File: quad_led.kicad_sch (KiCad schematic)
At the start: 8 parts

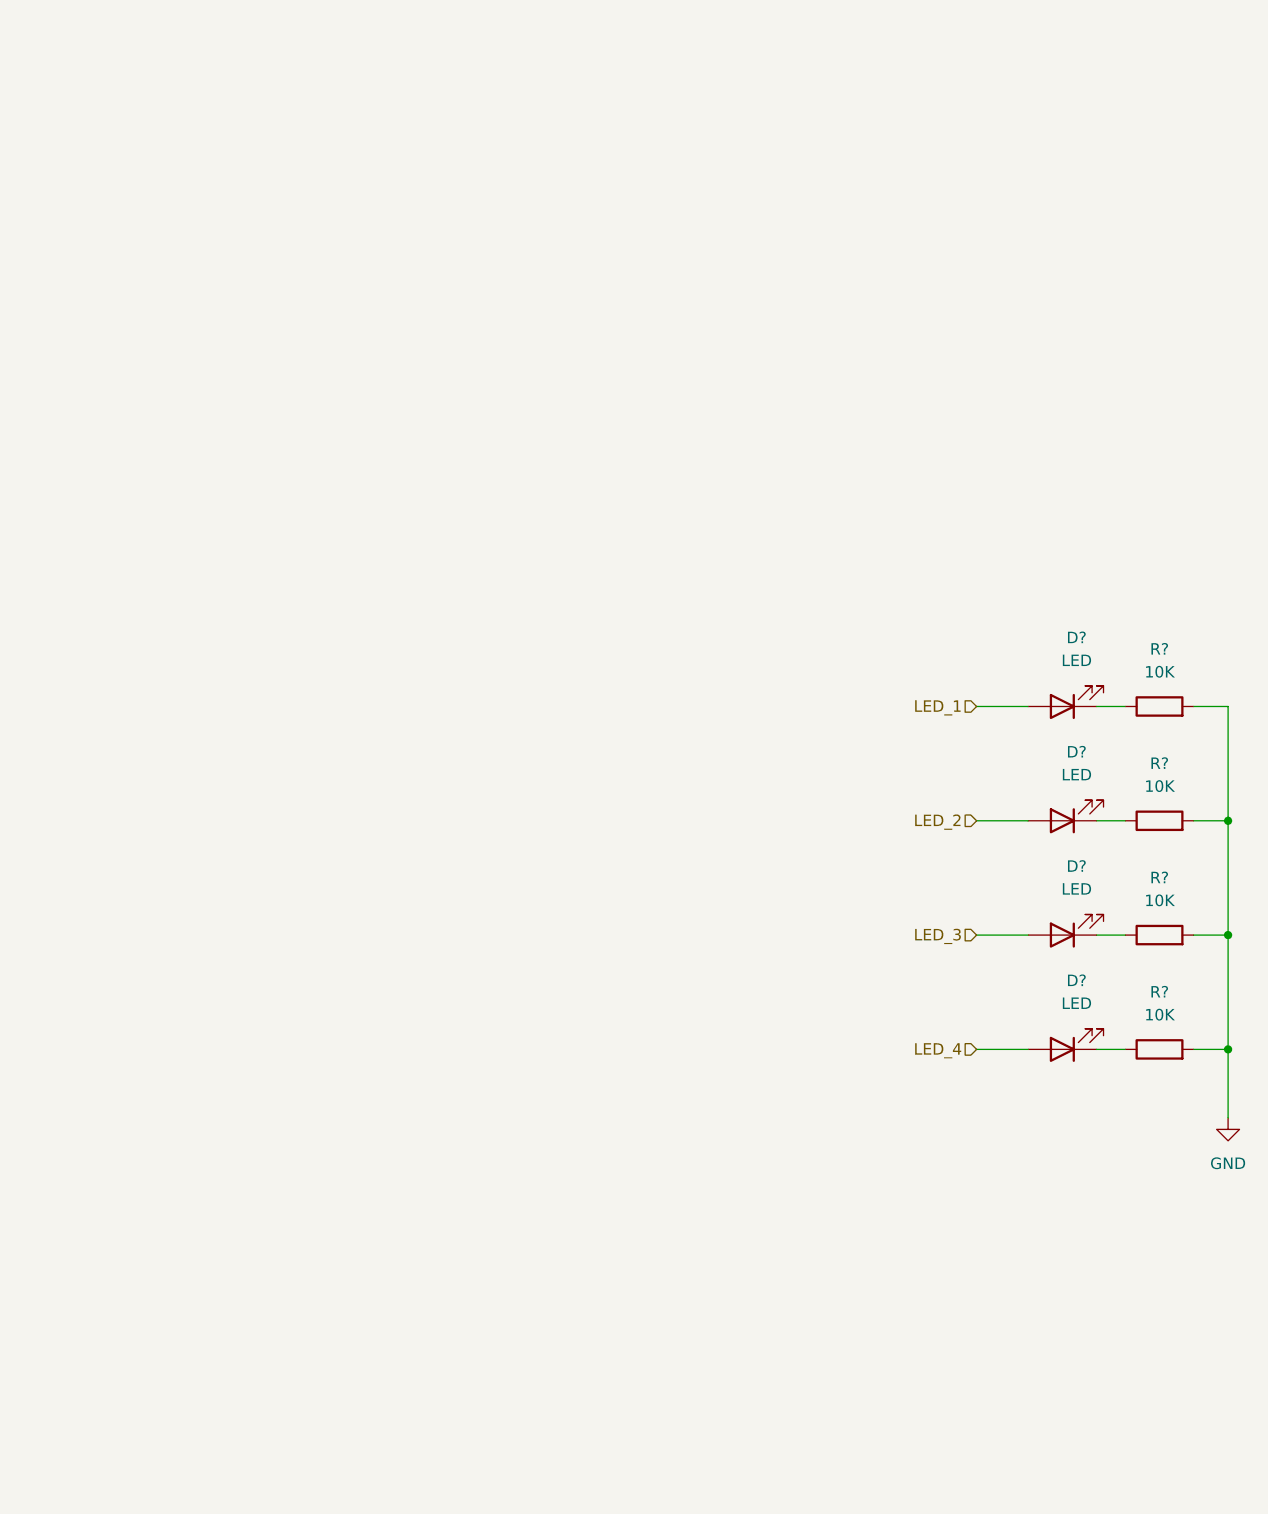
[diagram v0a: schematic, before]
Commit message: Review fixes
- swapped to HC components
- removed ctn_enable
- all 12 LEDs merged into 1 sheet
- No more error with the electrical checker
- various style improvements
- Introduce sleep deprivation errors like calling tranceivers d flip flops
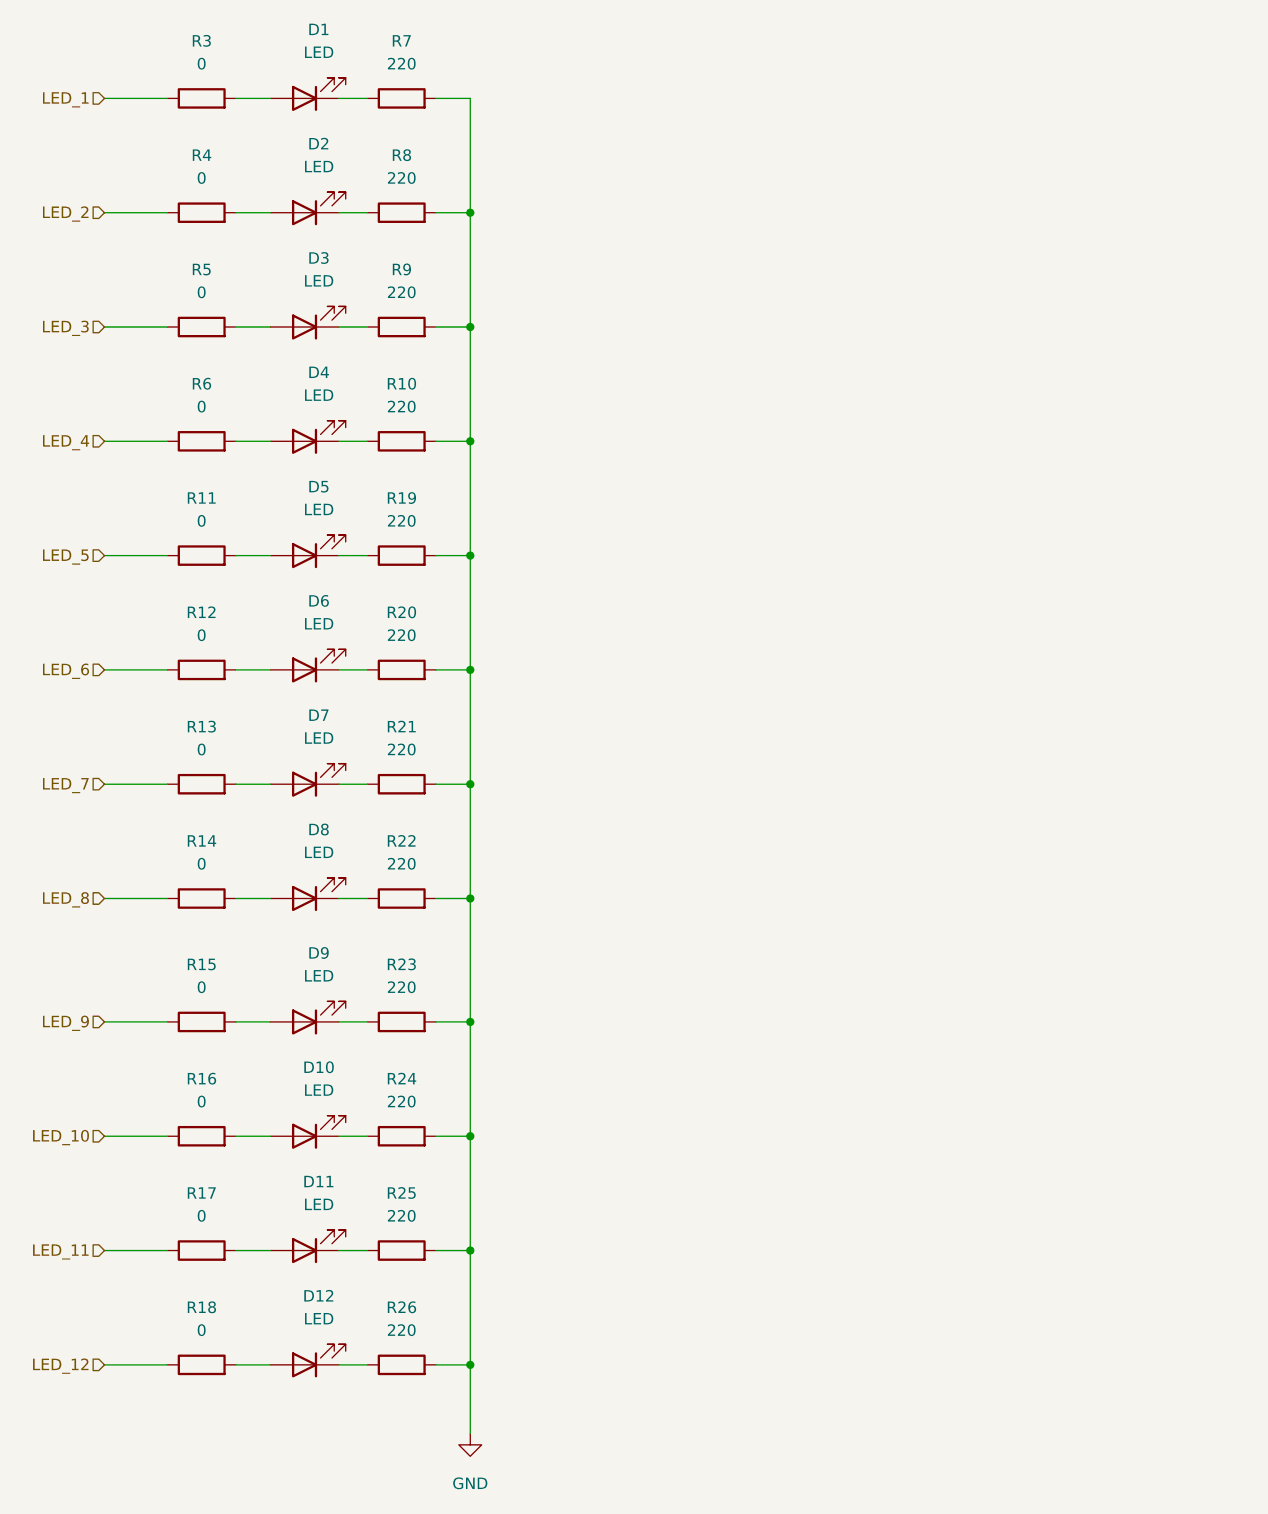
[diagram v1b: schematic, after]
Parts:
- added D10, D11, D12, D5, D6, D7, D8, D9: LED, symbol Device:LED
- added R11, R12, R13, R14, R15, R16, R17, R18, R3, R4, R5, R6: 0, symbol Device:R
- added R19, R20, R21, R22, R23, R24, R25, R26: 220, symbol Device:R
- R10, R7, R8, R9: renamed from R?; value 10K -> 220
- gave numbers to parts that had none: 4
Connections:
- net GND: now also R19.2, R20.2, R21.2, R22.2, R23.2, R24.2, R25.2, R26.2
- net LED_1: now also R3.1; no longer D1.2 (A)
- net LED_2: now also R4.1; no longer D2.2 (A)
- net LED_3: now also R5.1; no longer D3.2 (A)
- net LED_4: now also R6.1; no longer D4.2 (A)
- new net: D9.2 (A), R15.2
- new net: D1.2 (A), R3.2
- new net: D10.1 (K), R24.1
- new net: D2.2 (A), R4.2
- new net: D3.2 (A), R5.2
- new net: D12.2 (A), R18.2
- new net: D12.1 (K), R26.1
- new net: D10.2 (A), R16.2
- new net: D11.1 (K), R25.1
- new net: D8.1 (K), R22.1
- new net: D5.1 (K), R19.1
- new net: D8.2 (A), R14.2
- new net: D6.1 (K), R20.1
- new net: D9.1 (K), R23.1
- new net: D6.2 (A), R12.2
- new net: D5.2 (A), R11.2
- new net: D11.2 (A), R17.2
- new net: D4.2 (A), R6.2
- new net: D7.2 (A), R13.2
- new net: D7.1 (K), R21.1
- new net LED_10: R16.1
- new net LED_11: R17.1
- new net LED_12: R18.1
- new net LED_5: R11.1
- new net LED_6: R12.1
- new net LED_7: R13.1
- new net LED_8: R14.1
- new net LED_9: R15.1
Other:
- moved on the sheet: D1, D2, D3, D4, R10, R7, R8, R9

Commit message: Trace the layout
- Place components on PCB
- Add silkscreeen
- Add traces
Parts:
- removed R11, R12, R13, R14, R15, R16, R17, R18, R3, R4, R5, R6: 0, symbol Device:R
- D1, D10, D11, D12, D2, D3, D4, D5, D6, D7, D8, D9: footprint (none) -> Custom_lib:LED_1206_3216Metric_Pad1.42x1.75mm_HandSolder
- R10, R19, R20, R21, R22, R23, R24, R25, R26, R7, R8, R9: footprint (none) -> Resistor_SMD:R_1206_3216Metric_Pad1.30x1.75mm_HandSolder
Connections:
- net LED_1: now also D1.2 (A)
- net LED_10: now also D10.2 (A)
- net LED_11: now also D11.2 (A)
- net LED_12: now also D12.2 (A)
- net LED_2: now also D2.2 (A)
- net LED_3: now also D3.2 (A)
- net LED_4: now also D4.2 (A)
- net LED_5: now also D5.2 (A)
- net LED_6: now also D6.2 (A)
- net LED_7: now also D7.2 (A)
- net LED_8: now also D8.2 (A)
- net LED_9: now also D9.2 (A)
